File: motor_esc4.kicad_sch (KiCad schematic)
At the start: 12 parts, among them U7 MCF8316A

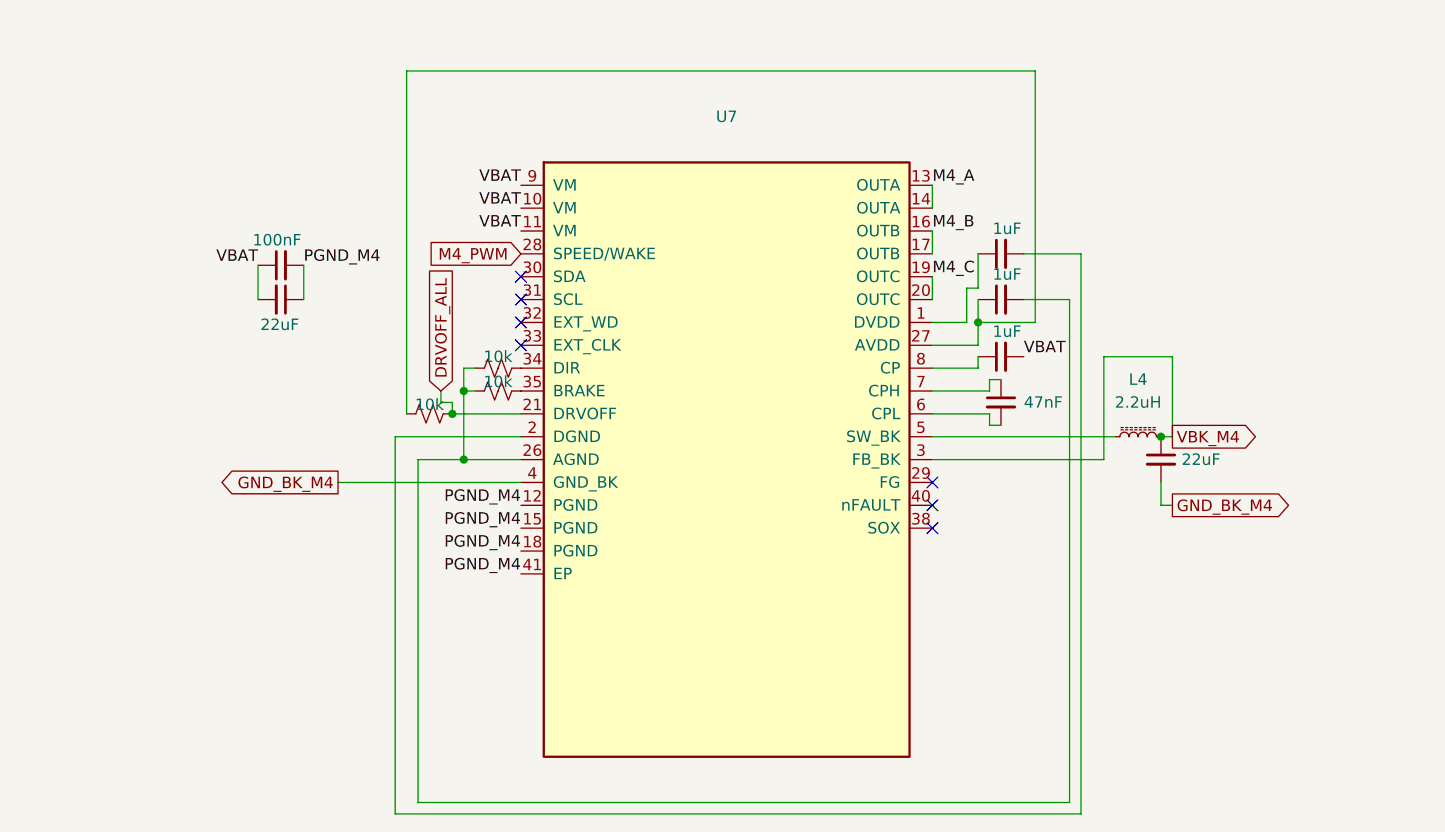
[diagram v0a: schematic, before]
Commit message: A LOT of changes, current state is 2 of 4 ESCs routed, power revamped. \n Board almost done
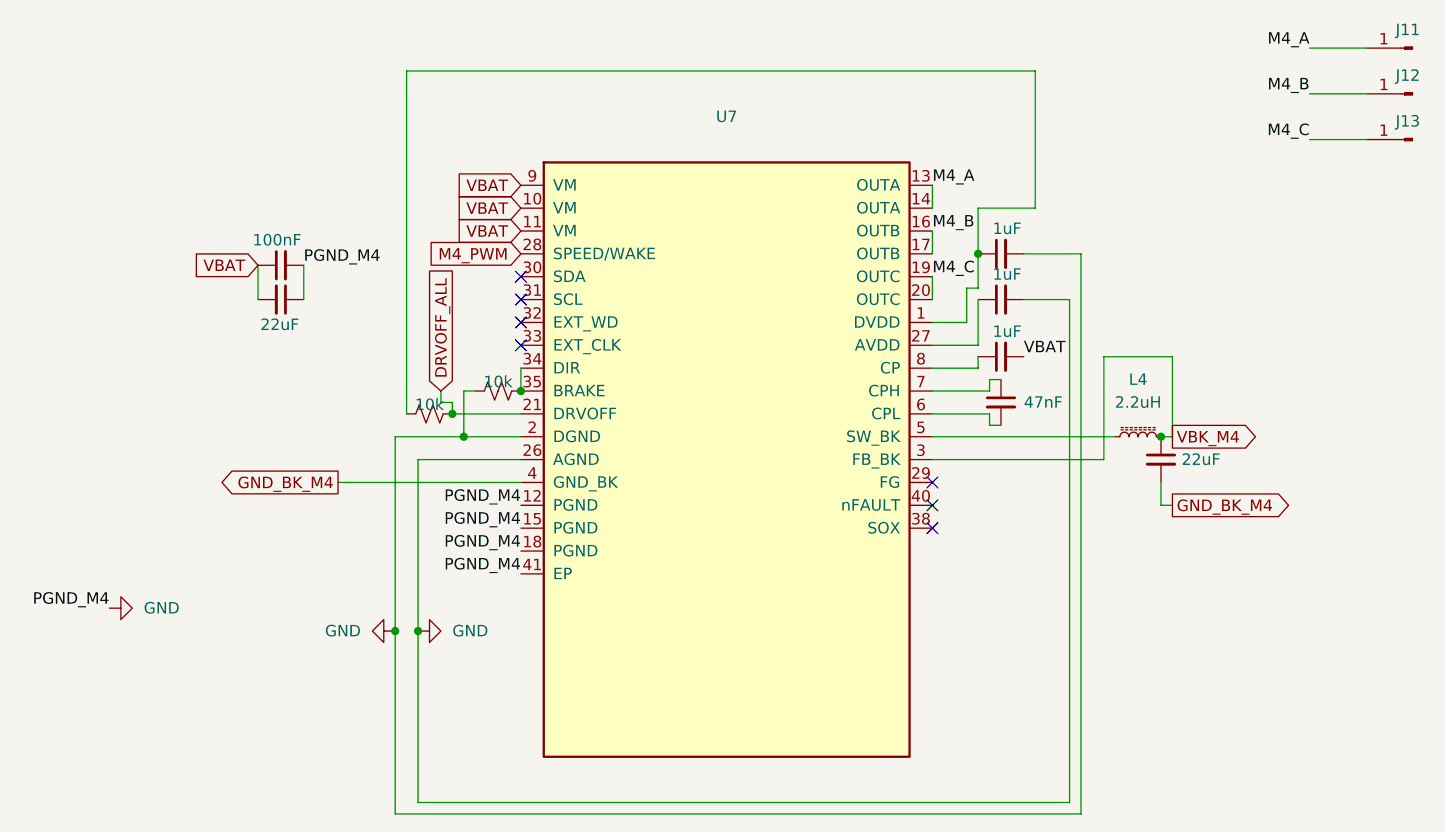
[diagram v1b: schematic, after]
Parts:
- removed R14: 10k, Resistor_SMD:R_0603_1608Metric_Pad0.98x0.95mm_HandSolder, symbol Device:R_Small_US
- added J11, J12, J13: SolderWirePad_1x01_SMD_3x6mm, Connector_Wire:SolderWirePad_1x01_SMD_3x6mm, symbol Connector:Conn_01x01_Pin
- U7: footprint MCF8316:MCF8316A_RGF0040E_VQFN-40-1EP_7x5mm_P0.5mm_EP5.5x3.5mm_kicad5_fixed_rotation -> MCF8316:MCF8316A_RGF0040E_VQFN-40-1EP_7x5mm_P0.5mm_EP5.5x3.5mm
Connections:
- net PGND_M4 is gone; now on net GND: C35.2, C36.1, U7.12 (PGND), U7.15 (PGND), U7.18 (PGND), U7.41 (EP)
- net M4_A: now also J11.1 (Pin_1)
- net M4_B: now also J12.1 (Pin_1)
- net M4_C: now also J13.1 (Pin_1)
- net at C38.1, U7.27 (AVDD): no longer R13.1
- net at C37.1, U7.1 (DVDD): now also R13.1
- net GND: now reaches C37.2, U7.2 (DGND)
- net GND: now also C38.2, R15.1, U7.26 (AGND)
- net at U7.34 (DIR): now also R15.2, U7.35 (BRAKE)

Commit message: done?
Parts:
- removed R13: 10k, Resistor_SMD:R_0603_1608Metric_Pad0.98x0.95mm_HandSolder, symbol Device:R_Small_US
- R15: footprint Resistor_SMD:R_0603_1608Metric_Pad0.98x0.95mm_HandSolder -> Resistor_SMD:R_0402_1005Metric_Pad0.72x0.64mm_HandSolder
